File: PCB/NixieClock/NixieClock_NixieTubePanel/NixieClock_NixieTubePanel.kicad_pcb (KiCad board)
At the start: 2 copper layers, 112 x 112 mm, 30 parts, among them J3 Conn_01x04_Pin, J4 Conn_01x04_Pin, U1 K155ID1, U2 K155ID1, U3 K155ID1, U4 K155ID1, U5 PCF8574, U6 PCF8574, X1 5230, X2 5230, X3 5230, X4 5230, X5 5230, X6 5230

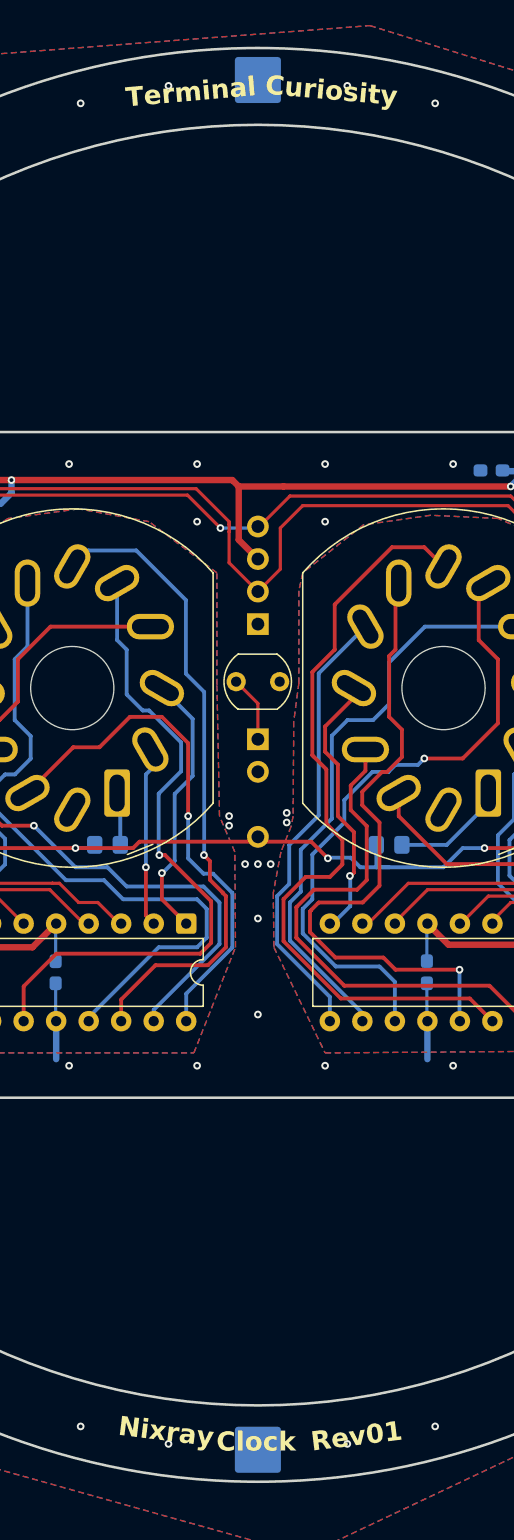
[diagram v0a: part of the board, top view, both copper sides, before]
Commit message: tidy labels and adjacent vias
aligned silkscreen labels and moved nearby vias to not conflict
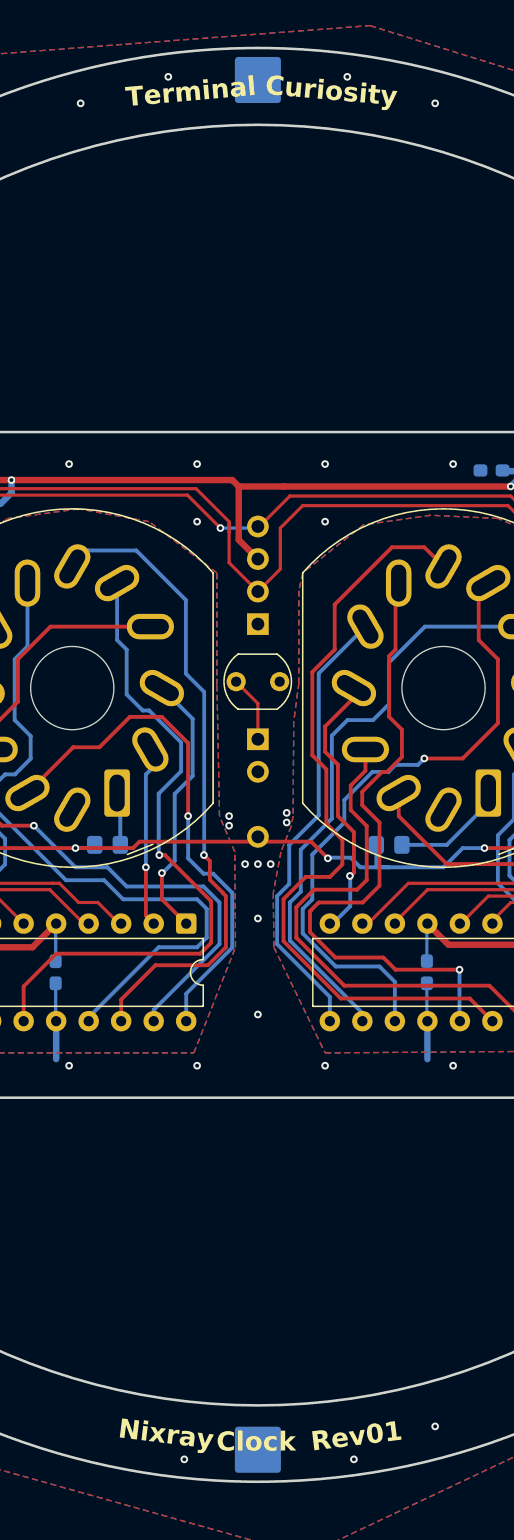
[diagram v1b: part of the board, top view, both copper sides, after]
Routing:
- net GND: vias 74 -> 73
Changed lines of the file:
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@@
 	)
 	(gr_text "Curiosity"
-		(at 130.5 47.75 355)
+		(at 130.5 47.77 355)
 		(layer "F.SilkS")
 		(effects
@@
 	)
 	(gr_text "Nixray"
-		(at 119 152.5 353)
+		(at 119 152.7 353)
 		(layer "F.SilkS")
 		(effects
@@
 	)
 	(gr_text "Terminal"
-		(at 119.75 48.75 5)
+		(at 119.75 48.73 5)
 		(layer "F.SilkS")
 		(effects
@@
 	)
 	(via
-		(at 116.153181 151.677032)
-		(size 0.6)
-		(drill 0.3)
-		(layers "F.Cu" "B.Cu")
-		(teardrops
-			(best_length_ratio 0.5)
-			(max_length 1)
-			(best_width_ratio 1)
-			(max_width 2)
-			(curved_edges no)
-			(filter_ratio 0.9)
-			(enabled yes)
-			(allow_two_segments yes)
-			(prefer_zone_connections yes)
-		)
-		(net 1)
-	)
-	(via
 		(at 165.25 76.5)
 		(size 0.6)
@@
 	)
 	(via
-		(at 136.983151 46.9577)
+		(at 136.983151 46.25)
 		(size 0.6)
 		(drill 0.3)
@@
 	)
 	(via
-		(at 136.983151 153.0423)
+		(at 137.5 154.25)
 		(size 0.6)
 		(drill 0.3)
@@
 	)
 	(via
-		(at 123.016849 46.9577)
+		(at 123 46.25)
 		(size 0.6)
 		(drill 0.3)
@@
 	)
 	(via
-		(at 123.016849 153.0423)
-		(size 0.6)
-		(drill 0.3)
+		(at 124.25 154.25)
+		(size 0.6)
+		(drill 0.3)

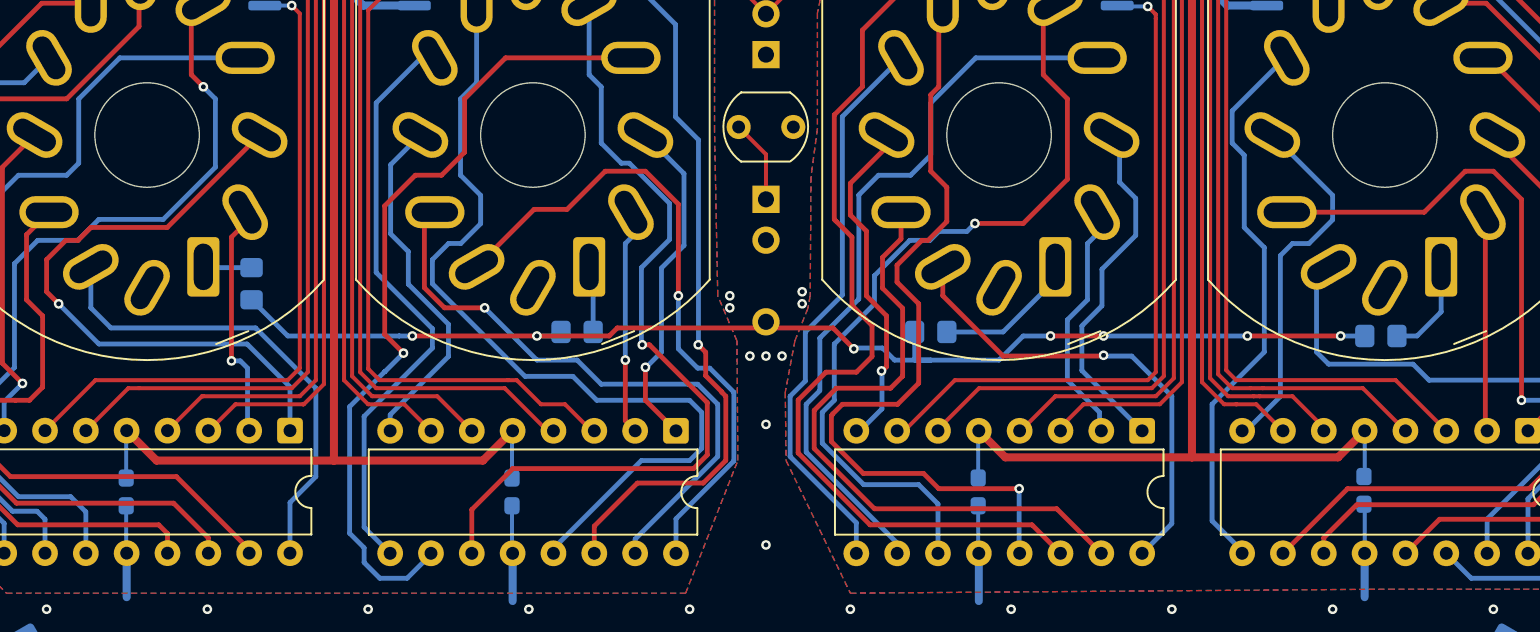
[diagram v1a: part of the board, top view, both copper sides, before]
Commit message: Change anode resistors from 0805 to 1206 for increased power headroom
changed resistors and adjusted traces to suit.
0805 resistors have Pmax 0.125W. if the PSU drifts up to 180-185V, it may exceed this power rating.
1206 doubles the headroom
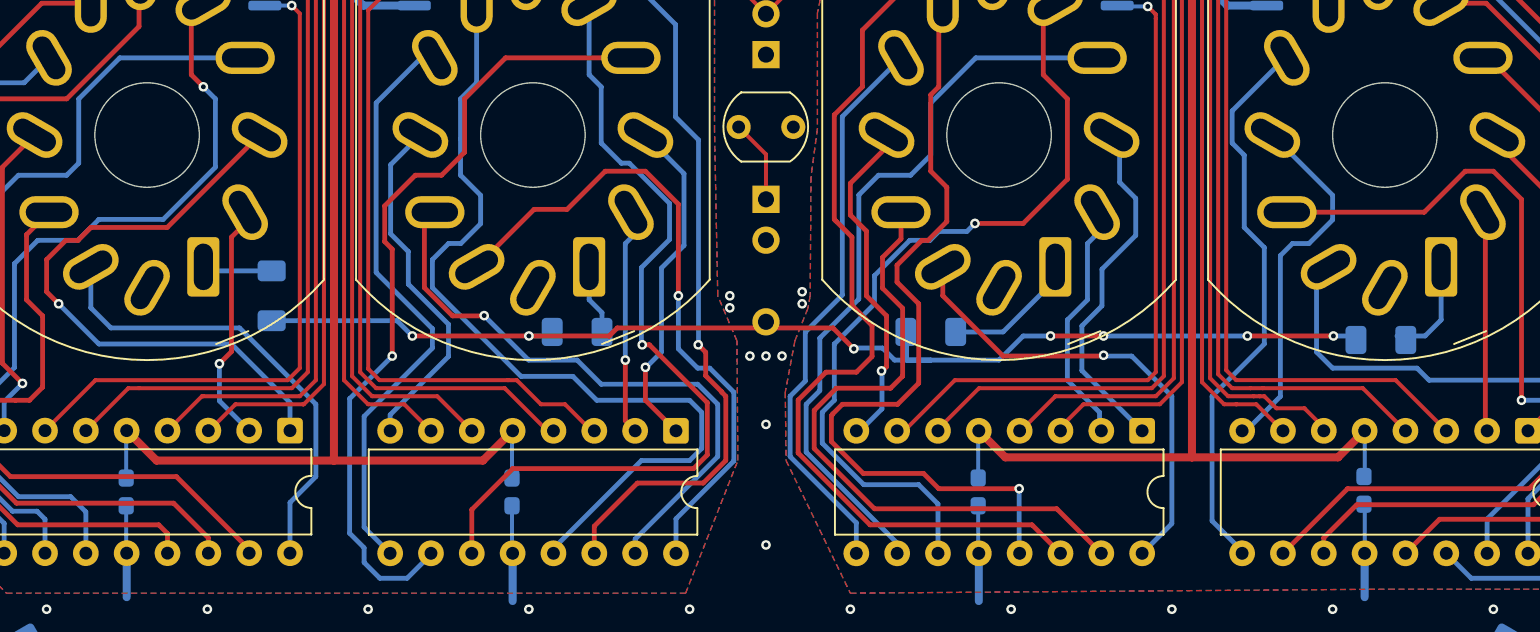
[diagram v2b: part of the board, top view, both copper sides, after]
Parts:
- R10, R11, R16, R9: footprint Resistor_SMD:R_0805_2012Metric_Pad1.20x1.40mm_HandSolder -> Resistor_SMD:R_1206_3216Metric_Pad1.30x1.75mm_HandSolder
- R18: value LDR07 -> 10K
- moved R9 1.46 mm to (99.2, 104.0)
- moved R16 0.25 mm to (168.2, 106.8)
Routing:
- net Net-(N1-V+): track 3.37 -> 5.34 mm
- net /+170V: track 78.0 -> 76.4 mm
- net Net-(N2-V+): track 3.65 -> 4.38 mm
- net Net-(N2-'8'): track 50.9 -> 50.3 mm
- net Net-(N1-'1'): track 29.5 -> 29.0 mm
- net Net-(N1-'9'): track 37.7 -> 37.1 mm
- net Net-(N3-V+): track 9.32 -> 8.77 mm

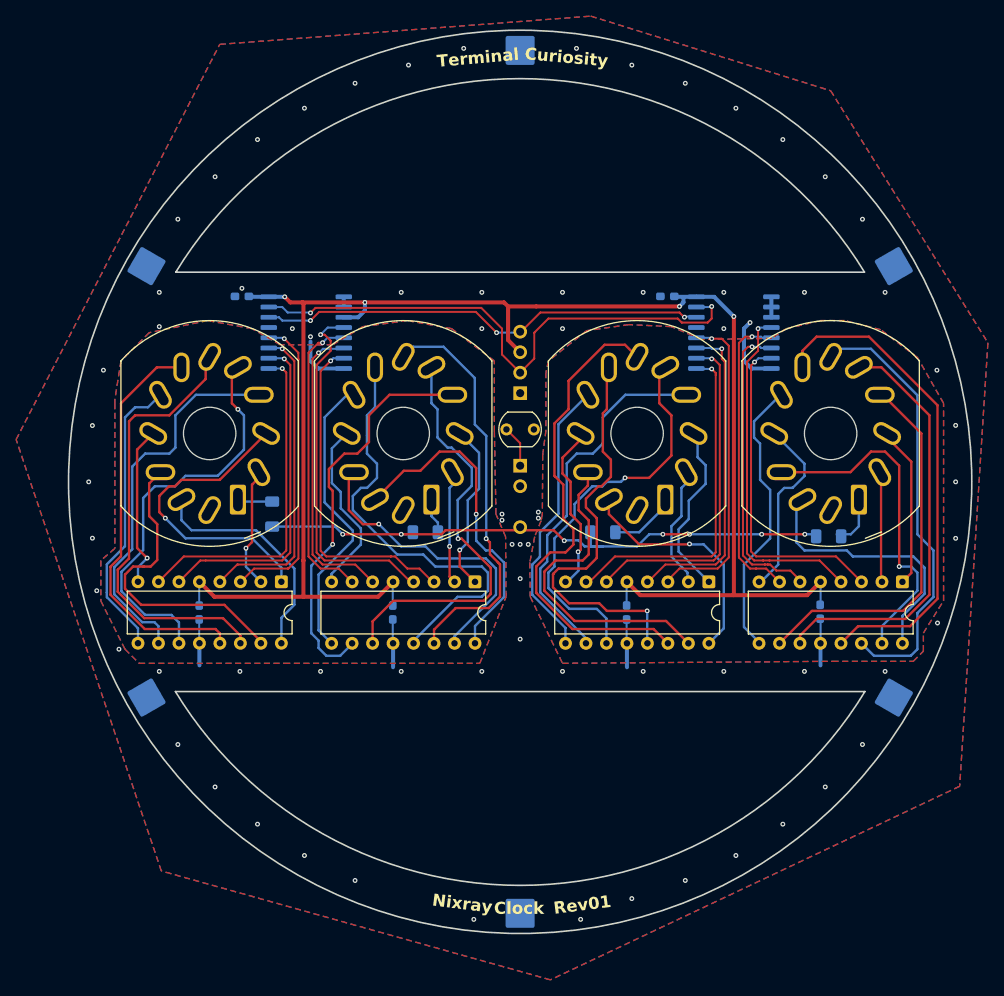
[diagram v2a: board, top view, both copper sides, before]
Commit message: decoupling caps 0603 -> 0805 for easier soldering
prototype feedback found that decoupling caps can be 0805 sized and easier to hand solder. 0603 is not required
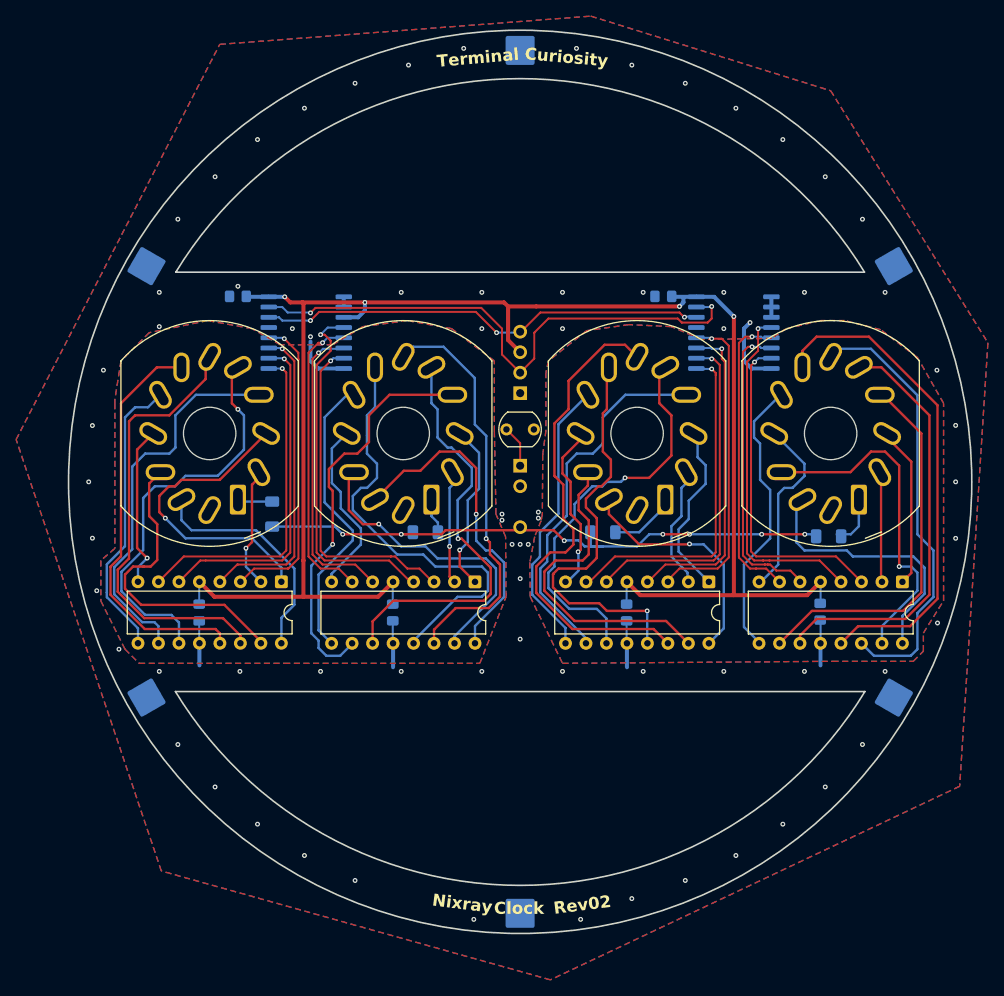
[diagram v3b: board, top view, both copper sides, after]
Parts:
- C10, C5, C6, C7, C8, C9: footprint Capacitor_SMD:C_0603_1608Metric_Pad1.08x0.95mm_HandSolder -> Capacitor_SMD:C_0805_2012Metric_Pad1.18x1.45mm_HandSolder
- moved C10 0.50 mm to (95.0, 77.0)
- moved C9 0.50 mm to (147.8, 77.0)
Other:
- board text added: "Rev02"
- board text removed: "Rev01"
